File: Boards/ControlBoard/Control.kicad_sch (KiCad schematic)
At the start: 38 parts, among them IC1 TXB0104DR, IC2 ADS8688AIDBT, IC4 TXB0104DR, IC5 TXB0104DR, IC7 TXB0104DR, IC8 TXB0104DR, J1 Conn_01x02_Pin

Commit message: Add Filter Caps To ADC Control Board IC
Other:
- note removed: "add filter caps here for all inputs"
- note removed: "check extra pins"
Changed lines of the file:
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@@
 	(generator_version "9.0")
 	(paper "A4")
-	(text "check extra pins"
-		(exclude_from_sim no)
-		(at 68.834 50.292 0)
-		(effects
-			(font
-				(size 1.27 1.27)
-			)
-			(justify left)
-		)
-	)
 	(text "UART Debug Header"
 		(exclude_from_sim no)
@@
 		)
 	)
-	(text "add filter caps here for all inputs"
-		(exclude_from_sim no)
-		(at 69.596 191.77 0)
-		(effects
-			(font
-				(size 1.27 1.27)
-			)
-			(justify left)
-		)
-	)

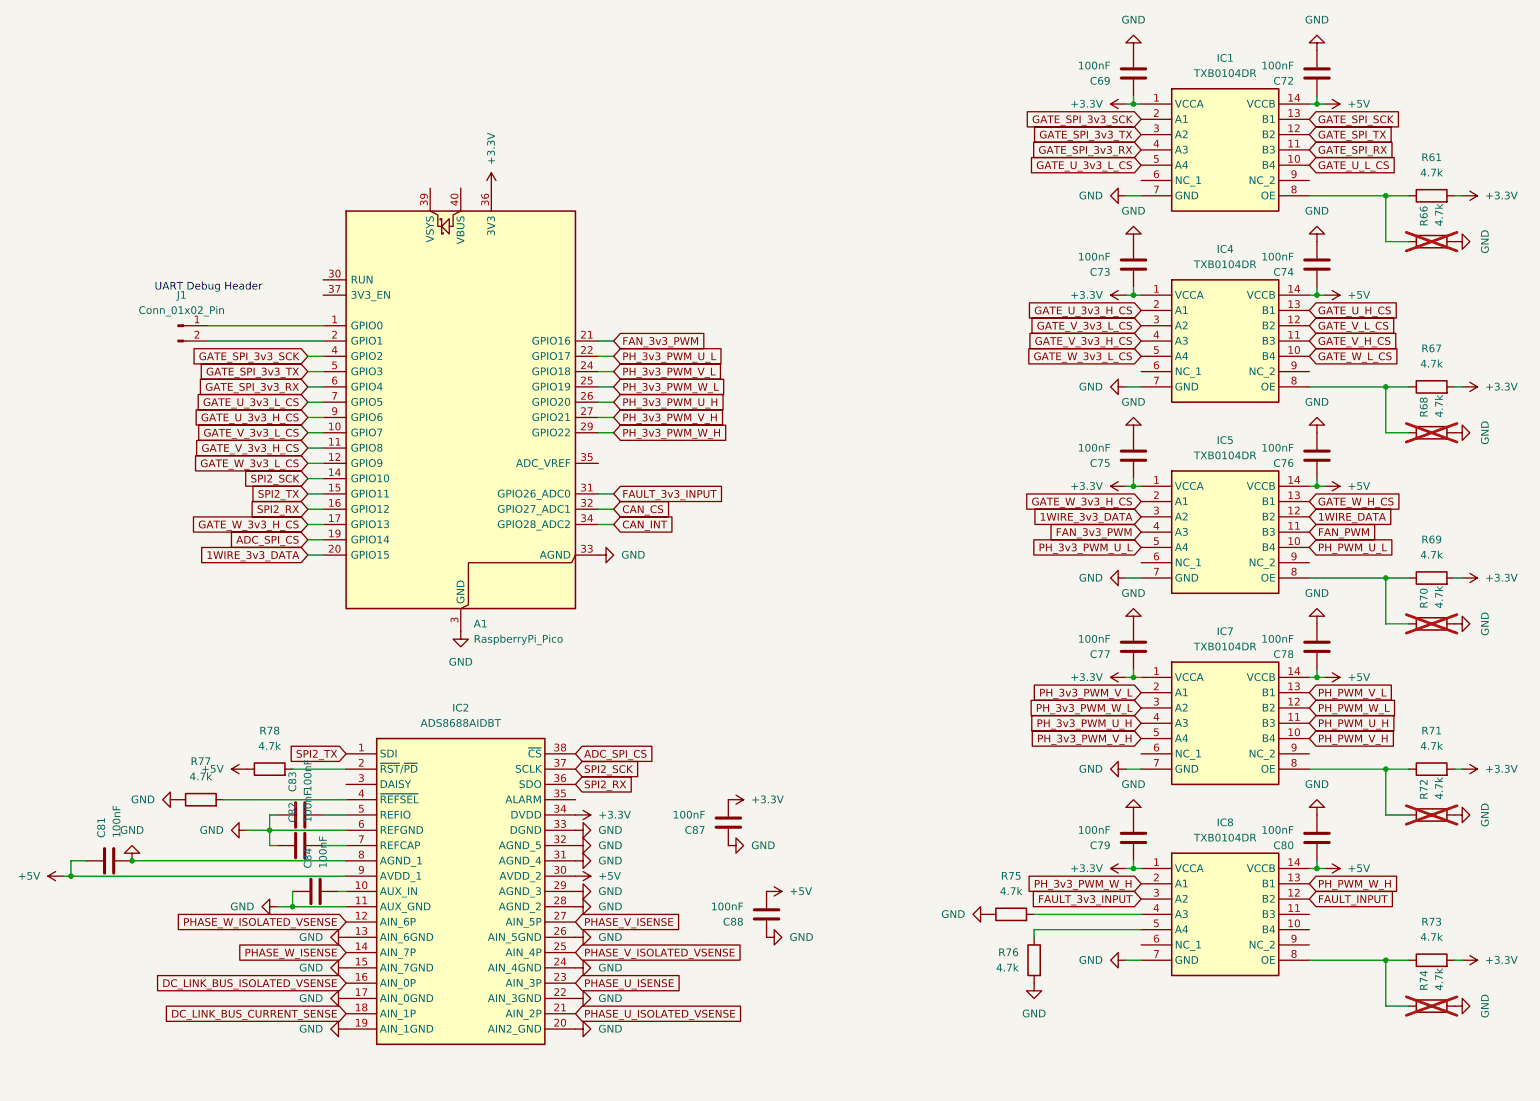
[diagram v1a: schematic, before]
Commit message: Update control board
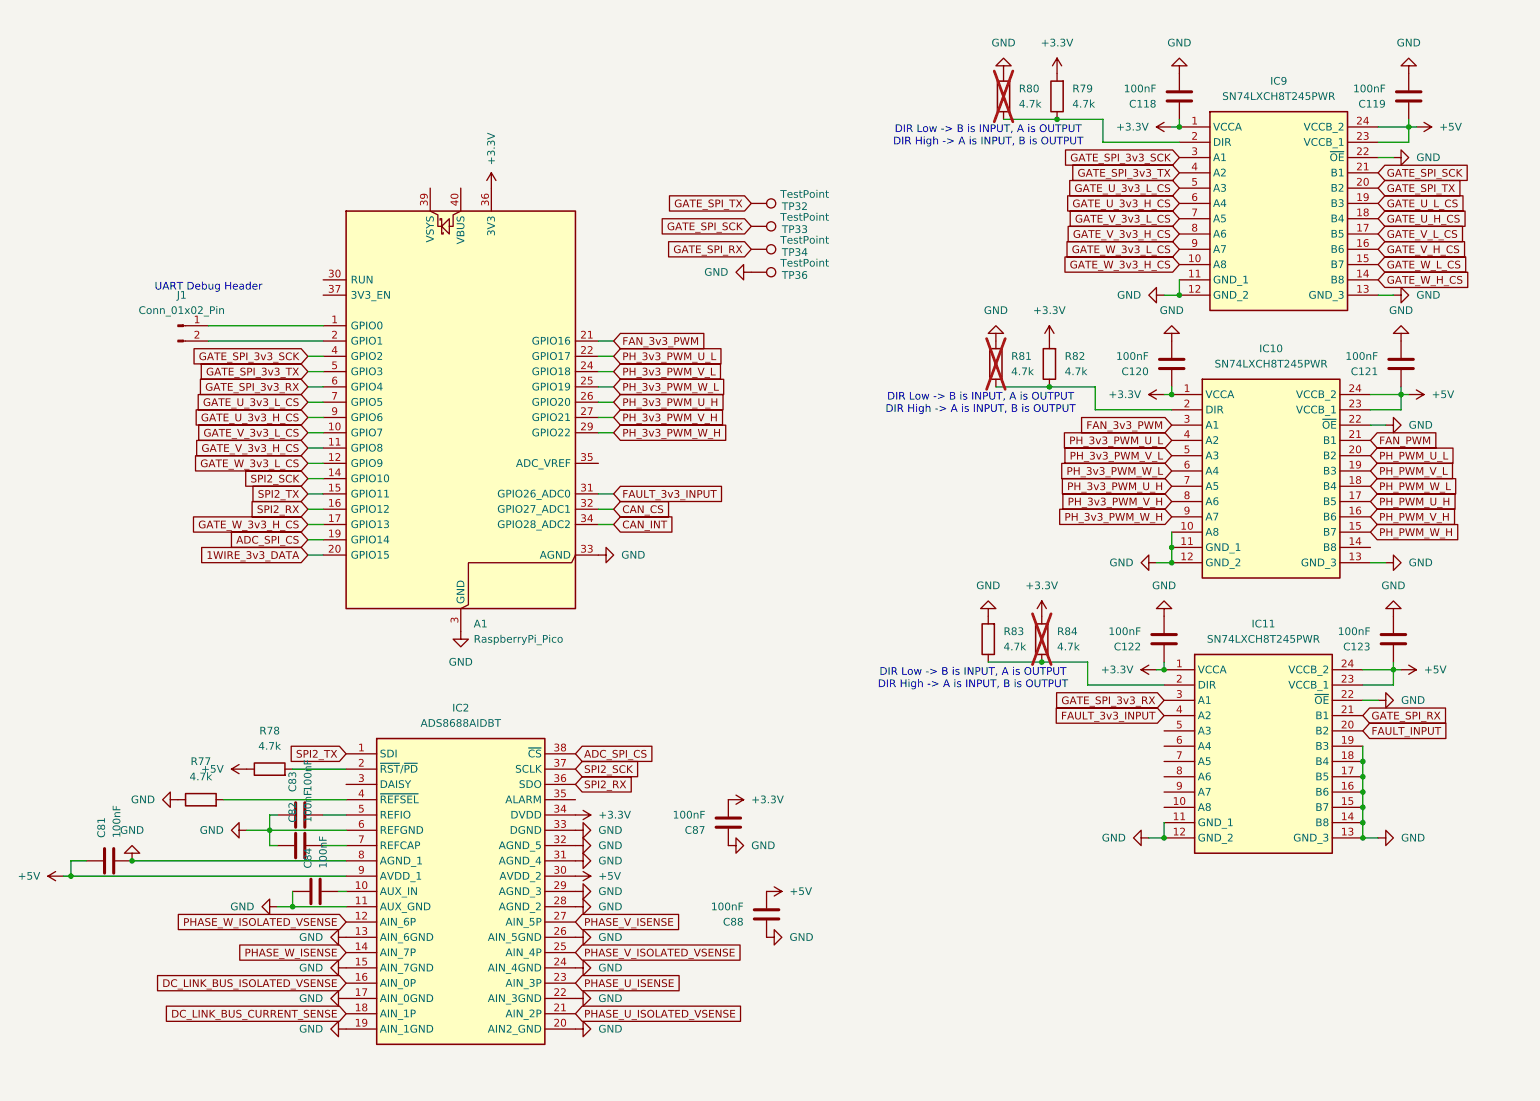
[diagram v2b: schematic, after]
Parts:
- removed C69, C72, C73, C74, C75, C76, C77, C78, C79, C80: 100nF, Capacitor_SMD:C_1210_3225Metric_Pad1.33x2.70mm_HandSolder, symbol Device:C
- removed IC1, IC4, IC5, IC7, IC8: TXB0104DR, InverterCom:SOIC127P600X175-14N, symbol InverterCom:TXB0104DR
- removed R61, R66, R67, R68, R69, R70, R71, R72, R73, R74, R75, R76: 4.7k, Resistor_SMD:R_1210_3225Metric_Pad1.30x2.65mm_HandSolder, symbol Device:R
- added C118, C119, C120, C121, C122, C123: 100nF, Capacitor_SMD:C_1210_3225Metric_Pad1.33x2.70mm_HandSolder, symbol Device:C
- added IC10, IC11, IC9: SN74LXCH8T245PWR, InverterCom:SOP65P640X120-24N, symbol InverterCom:SN74LXCH8T245PWR
- added R79, R80, R81, R82, R83, R84: 4.7k, Resistor_SMD:R_1210_3225Metric_Pad1.30x2.65mm_HandSolder, symbol Device:R
- added TP32, TP33, TP34, TP36: TestPoint, TestPoint:TestPoint_Loop_D2.54mm_Drill1.5mm_Beaded, symbol Connector:TestPoint
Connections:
- net +3.3V: now also C118.1, C120.1, C122.1, IC10.1 (VCCA), IC11.1 (VCCA), IC9.1 (VCCA), R79.2, R82.2, R84.2
- net +5V: now also C119.1, C121.1, C123.1, IC10.23 (VCCB_1), IC10.24 (VCCB_2), IC11.23 (VCCB_1), IC11.24 (VCCB_2), IC9.23 (VCCB_1), IC9.24 (VCCB_2)
- net FAN_3v3_PWM: now also IC10.3 (A1)
- net FAN_PWM: now also IC10.21 (B1)
- net FAULT_3v3_INPUT: now also IC11.4 (A2)
- net FAULT_INPUT: now also IC11.20 (B2)
- net GATE_SPI_3v3_RX: now also IC11.3 (A1)
- net GATE_SPI_3v3_SCK: now also IC9.3 (A1)
- net GATE_SPI_3v3_TX: now also IC9.4 (A2)
- net GATE_SPI_RX: now also IC11.21 (B1), TP34.1
- net GATE_SPI_SCK: now also IC9.21 (B1), TP33.1
- net GATE_SPI_TX: now also IC9.20 (B2), TP32.1
- net GATE_U_3v3_H_CS: now also IC9.6 (A4)
- net GATE_U_3v3_L_CS: now also IC9.5 (A3)
- net GATE_U_H_CS: now also IC9.18 (B4)
- net GATE_U_L_CS: now also IC9.19 (B3)
- net GATE_V_3v3_H_CS: now also IC9.8 (A6)
- net GATE_V_3v3_L_CS: now also IC9.7 (A5)
- net GATE_V_H_CS: now also IC9.16 (B6)
- net GATE_V_L_CS: now also IC9.17 (B5)
- net GATE_W_3v3_H_CS: now also IC9.10 (A8)
- net GATE_W_3v3_L_CS: now also IC9.9 (A7)
- net GATE_W_H_CS: now also IC9.14 (B8)
- net GATE_W_L_CS: now also IC9.15 (B7)
- net GND: now also C118.2, C119.2, C120.2, C121.2, C122.2, C123.2, IC10.10 (A8), IC10.11 (GND_1), IC10.12 (GND_2), IC10.13 (GND_3), IC10.22 (~{OE}), IC11.11 (GND_1), IC11.12 (GND_2), IC11.13 (GND_3), IC11.14 (B8), IC11.15 (B7), IC11.16 (B6), IC11.17 (B5), IC11.18 (B4), IC11.19 (B3), IC11.22 (~{OE}), IC9.11 (GND_1), IC9.12 (GND_2), IC9.13 (GND_3), IC9.22 (~{OE}), R80.2, R81.2, R83.2, TP36.1
- net PH_3v3_PWM_U_H: now also IC10.7 (A5)
- net PH_3v3_PWM_U_L: now also IC10.4 (A2)
- net PH_3v3_PWM_V_H: now also IC10.8 (A6)
- net PH_3v3_PWM_V_L: now also IC10.5 (A3)
- net PH_3v3_PWM_W_H: now also IC10.9 (A7)
- net PH_3v3_PWM_W_L: now also IC10.6 (A4)
- net PH_PWM_U_H: now also IC10.17 (B5)
- net PH_PWM_U_L: now also IC10.20 (B2)
- net PH_PWM_V_H: now also IC10.16 (B6)
- net PH_PWM_V_L: now also IC10.19 (B3)
- net PH_PWM_W_H: now also IC10.15 (B7)
- net PH_PWM_W_L: now also IC10.18 (B4)
- new net: IC11.2 (DIR), R83.1, R84.1
- new net: IC9.2 (DIR), R79.1, R80.1
- new net: IC10.2 (DIR), R81.1, R82.1
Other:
- note added: "DIR Low -> B is INPUT, A is OUTPUT DIR High -> A is INPUT, B is OUTPUT"
